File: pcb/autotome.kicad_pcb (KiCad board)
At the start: 2 copper layers, 61 parts, among them SW1 SW_PUSH, SW10 SW_PUSH, SW11 SW_PUSH, SW12 SW_PUSH, SW13 SW_PUSH, SW14 SW_PUSH, SW15 SW_PUSH, SW16 SW_PUSH, SW17 SW_PUSH, SW18 SW_PUSH, SW19 SW_PUSH, SW2 SW_PUSH, SW20 SW_PUSH, SW21 SW_PUSH, SW22 SW_PUSH, SW23 SW_PUSH, SW24 SW_PUSH, SW25 RotaryEncoder_Switch, SW27 SW_PUSH, SW28 SW_PUSH, SW29 SW_PUSH, SW3 SW_PUSH, SW30 SW_PUSH, SW31 SW_SPDT, SW4 SW_PUSH, SW5 SW_PUSH, SW6 SW_PUSH, SW7 SW_PUSH, SW8 SW_PUSH, SW9 SW_PUSH, U1 ProMicro

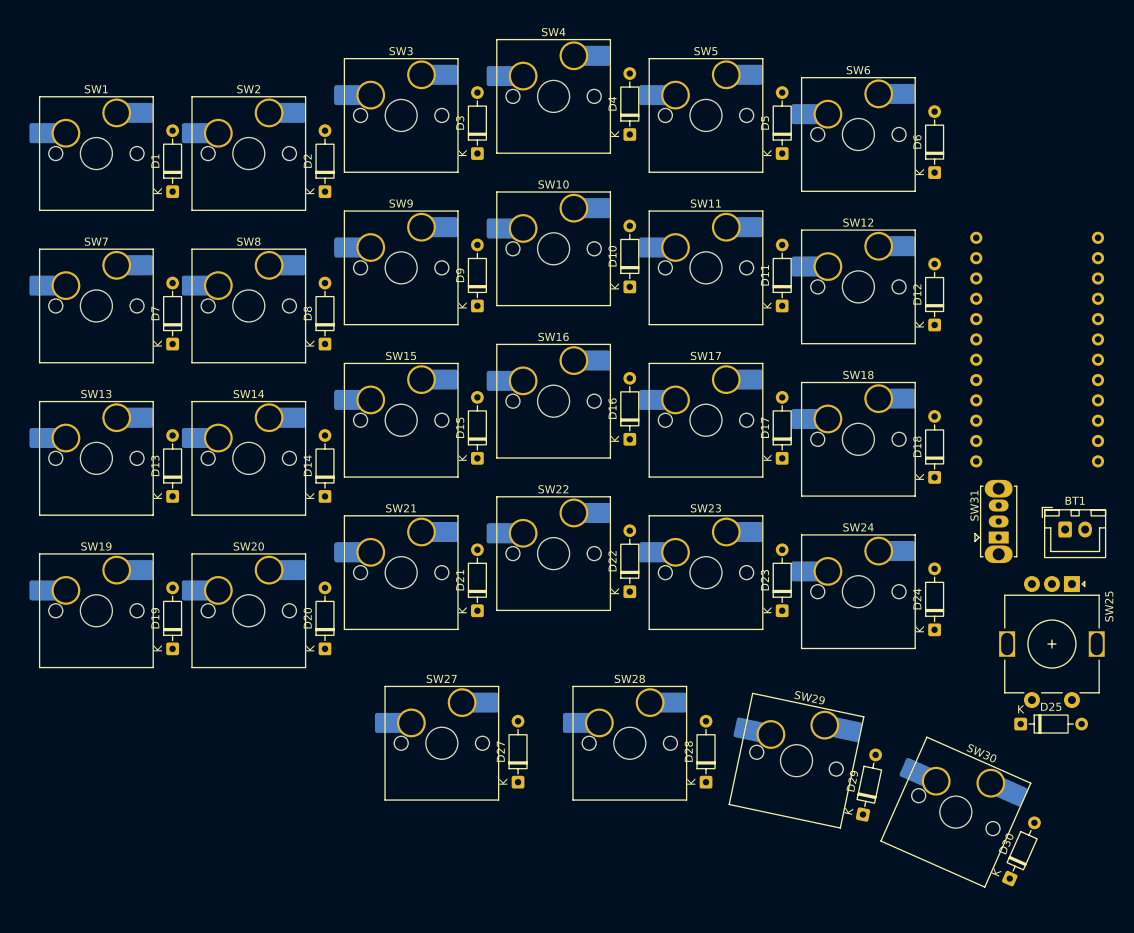
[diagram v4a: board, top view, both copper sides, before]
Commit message: add board outline at .5mm offset
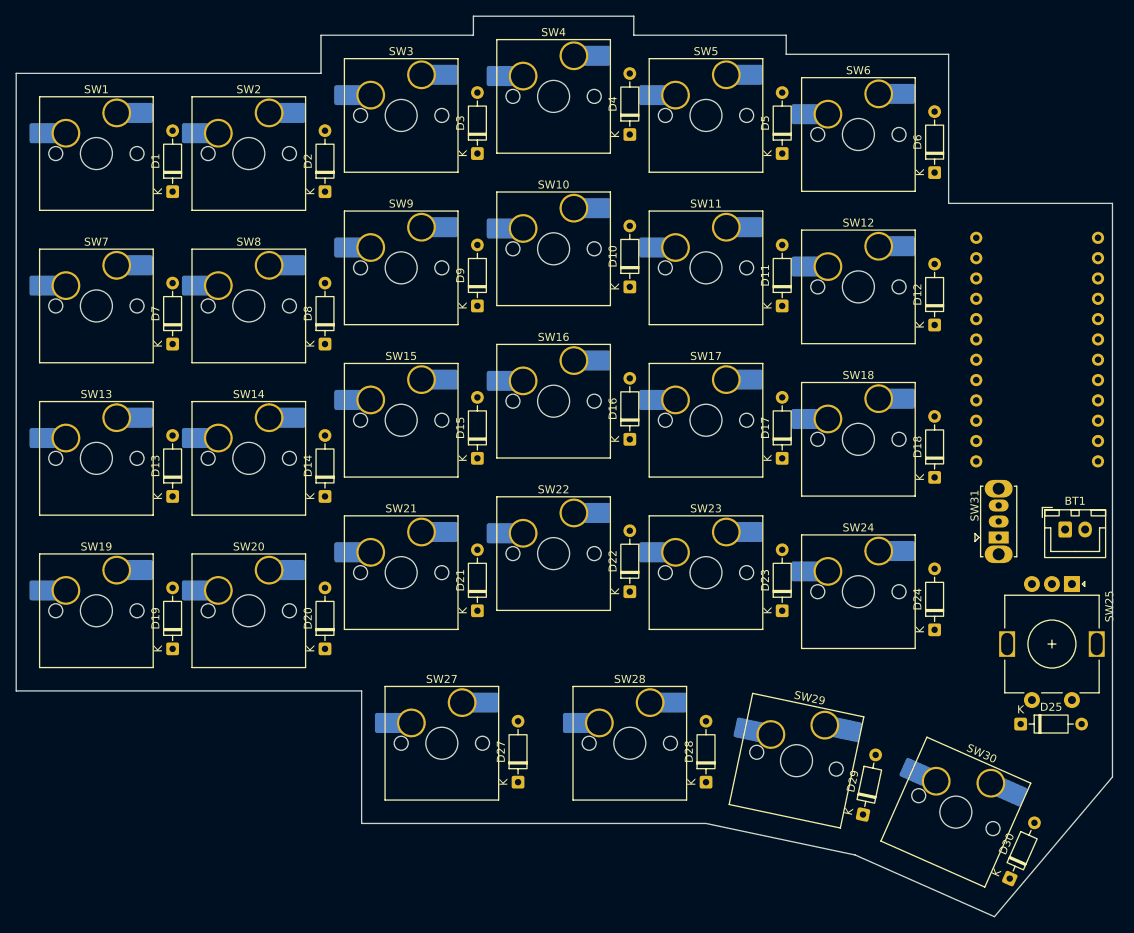
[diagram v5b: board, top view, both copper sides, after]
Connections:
- SW31 pad 1: Net-(BT1-+) -> unconnected-(SW31-A-Pad1)
- SW31 pad 2: unconnected-(SW31-B-Pad2) -> Net-(BT1-+)
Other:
- board outline added: 137 x 112.6 mm
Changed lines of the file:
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@@
 		(capping no)
 		(filling no)
-		(aux_axis_origin 123.14608 139.584744)
+		(grid_origin 136.967258 59.116053)
 		(pcbplotparams
 			(layerselection 0x00000000_00000000_55555555_5755f5ff)
@@
 		(duplicate_pad_numbers_are_jumpers no)
 		(fp_line
-			(start 2.289999 -1.12)
+			(start 2.289998 -1.12)
 			(end 2.290001 1.12)
 			(stroke
@@
 		(fp_line
 			(start 0 0)
-			(end 1.81 0.000001)
+			(end 1.81 0.000002)
 			(stroke
 				(width 0.1)
@@
 		)
 		(fp_line
-			(start -6.999999 7.000001)
+			(start -6.999999 7.000002)
 			(end -7 6)
 			(stroke
@@
 		(fp_line
 			(start -7 -6)
-			(end -7.000001 -6.999999)
+			(end -7.000002 -6.999999)
 			(stroke
 				(width 0.1)
@@
 		)
 		(fp_line
-			(start -7.000001 -6.999999)
-			(end 6.999999 -7.000001)
+			(start -7.000002 -6.999999)
+			(end 6.999999 -7.000002)
 			(stroke
 				(width 0.1)
@@
 		)
 		(fp_line
-			(start 7.000001 6.999999)
-			(end -6.999999 7.000001)
+			(start 7.000002 6.999999)
+			(end -6.999999 7.000002)
 			(stroke
 				(width 0.1)
@@
 		(fp_line
 			(start 7 6)
-			(end 7.000001 6.999999)
+			(end 7.000002 6.999999)
 			(stroke
 				(width 0.1)
@@
 		)
 		(fp_line
-			(start 6.999999 -7.000001)
+			(start 6.999999 -7.000002)
 			(end 7 -6)
 			(stroke
@@
 		)
 		(fp_line
-			(start -6.999999 7.000001)
-			(end 7.000001 6.999999)
+			(start -6.999999 7.000002)
+			(end 7.000002 6.999999)
 			(stroke
 				(width 0.1)
@@
 		)
 		(fp_line
-			(start -7.000001 -6.999999)
-			(end -6.999999 7.000001)
+			(start -7.000002 -6.999999)
+			(end -6.999999 7.000002)
 			(stroke
 				(width 0.1)
@@
 		)
 		(fp_line
-			(start 7.000001 6.999999)
-			(end 6.999999 -7.000001)
+			(start 7.000002 6.999999)
+			(end 6.999999 -7.000002)
 			(stroke
 				(width 0.1)
@@
 		)
 		(fp_line
-			(start 6.999999 -7.000001)
-			(end -7.000001 -6.999999)
+			(start 6.999999 -7.000002)
+			(end -7.000002 -6.999999)
 			(stroke
 				(width 0.1)
@@
 			(layers "*.Cu" "*.Mask")
 			(remove_unused_layers no)
-			(net "Net-(BT1-+)")
+			(net "unconnected-(SW31-A-Pad1)")
 			(pinfunction "A_1")
 			(pintype "passive")
@@
 			(layers "*.Cu" "*.Mask")
 			(remove_unused_layers no)
-			(net "unconnected-(SW31-B-Pad2)")
+			(net "Net-(BT1-+)")
 			(pinfunction "B_2")
 			(pintype "passive")
@@
 		(sheetname "/")
 		(sheetfile "autotome.kicad_sch")
+		(units
+			(unit
+				(name "A")
+				(pins "1" "2" "3" "4" "5" "6" "7" "8" "9" "10" "11" "12" "24" "23" "22"
+					"21" "20" "19" "18" "17" "16" "15" "14" "13"
+				)
+			)
+		)
 		(attr through_hole)
 		(duplicate_pad_numbers_are_jumpers no)
@@
 		)
 	)
+	(gr_line
+		(start 18.232504 42.362516)
+		(end 56.332504 42.362516)
+		(stroke
+			(width 0.05)
+			(type default)
+		)
+		(layer "Edge.Cuts")
+	)
+	(gr_line
+		(start 18.232504 119.562516)
+		(end 18.232504 42.362516)
+		(stroke
+			(width 0.05)
+			(type default)
+		)
+		(layer "Edge.Cuts")
+	)
+	(gr_line
+		(start 18.232504 119.562516)
+		(end 61.412503 119.562516)
+		(stroke
+			(width 0.05)
+			(type default)
+		)
+		(layer "Edge.Cuts")
+	)
+	(gr_line
+		(start 56.332504 37.599507)
+		(end 75.382498 37.599507)
+		(stroke
+			(width 0.05)
+			(type default)
+		)
+		(layer "Edge.Cuts")
+	)
+	(gr_line
+		(start 56.332504 42.362516)
+		(end 56.332504 37.599507)
+		(stroke
+			(width 0.05)
+			(type default)
+		)
+		(layer "Edge.Cuts")
+	)
+	(gr_line
+		(start 61.412503 119.562516)
+		(end 61.412503 136.125497)
+		(stroke
+			(width 0.05)
+			(type default)
+		)
+		(layer "Edge.Cuts")
+	)
+	(gr_line
+		(start 61.412503 136.125497)
+		(end 104.460011 136.125491)
+		(stroke
+			(width 0.05)
+			(type default)
+		)
+		(layer "Edge.Cuts")
+	)
+	(gr_line
+		(start 75.382503 35.218496)
+		(end 75.382498 37.599507)
+		(stroke
+			(width 0.05)
+			(type default)
+		)
+		(layer "Edge.Cuts")
+	)
+	(gr_line
+		(start 75.382503 35.218496)
+		(end 95.432503 35.218496)
+		(stroke
+			(width 0.05)
+			(type default)
+		)
+		(layer "Edge.Cuts")
+	)
+	(gr_line
+		(start 95.432498 37.599507)
+		(end 114.482498 37.599507)
+		(stroke
+			(width 0.05)
+			(type default)
+		)
+		(layer "Edge.Cuts")
+	)
+	(gr_line
+		(start 95.432503 35.218496)
+		(end 95.432498 37.599507)
+		(stroke
+			(width 0.05)
+			(type default)
+		)
+		(layer "Edge.Cuts")
+	)
+	(gr_line
+		(start 104.460011 136.125491)
+		(end 123.09786 140.066693)
+		(stroke
+			(width 0.05)
+			(type default)
+		)
+		(layer "Edge.Cuts")
+	)
+	(gr_line
+		(start 114.482498 37.599507)
+		(end 114.482515 39.980505)
+		(stroke
+			(width 0.05)
+			(type default)
+		)
+		(layer "Edge.Cuts")
+	)
+	(gr_line
+		(start 114.482515 39.980505)
+		(end 134.785011 39.980505)
+		(stroke
+			(width 0.05)
+			(type default)
+		)
+		(layer "Edge.Cuts")
+	)
+	(gr_line
+		(start 123.09786 140.066693)
+		(end 140.517091 147.77856)
+		(stroke
+			(width 0.05)
+			(type default)
+		)
+		(layer "Edge.Cuts")
+	)
+	(gr_line
+		(start 134.785011 39.980505)
+		(end 134.785011 58.616053)
+		(stroke
+			(width 0.05)
+			(type default)
+		)
+		(layer "Edge.Cuts")
+	)
+	(gr_line
+		(start 134.785011 58.616053)
+		(end 155.267258 58.616053)
+		(stroke
+			(width 0.05)
+			(type default)
+		)
+		(layer "Edge.Cuts")
+	)
+	(gr_line
+		(start 155.267258 58.616053)
+		(end 155.267258 130.316053)
+		(stroke
+			(width 0.05)
+			(type default)
+		)
+		(layer "Edge.Cuts")
+	)
+	(gr_line
+		(start 155.267258 130.316053)
+		(end 140.517091 147.77856)
+		(stroke
+			(width 0.05)
+			(type default)
+		)
+		(layer "Edge.Cuts")
+	)
 	(embedded_fonts no)

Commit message: add 1mm fillet
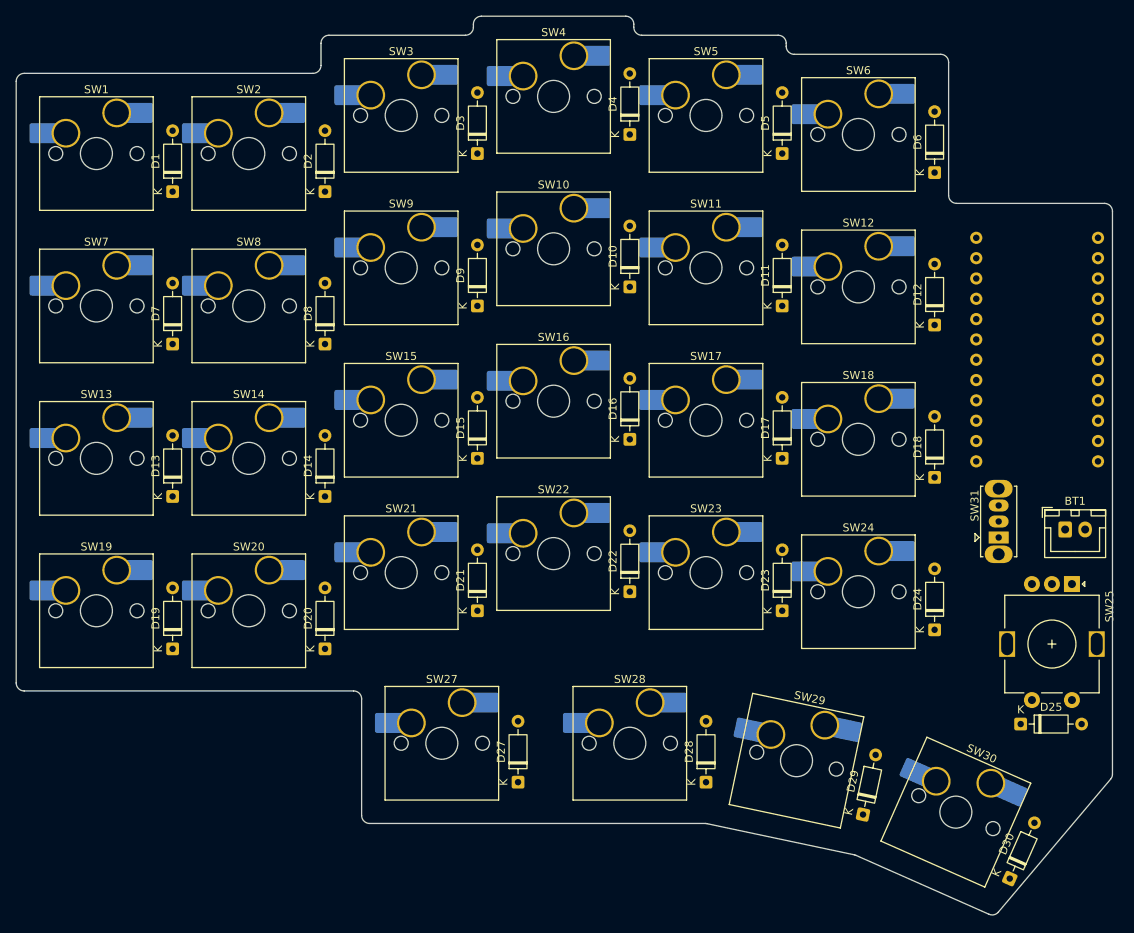
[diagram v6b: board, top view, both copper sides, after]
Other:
- board size 137 x 112.6 mm -> 137 x 112.3 mm

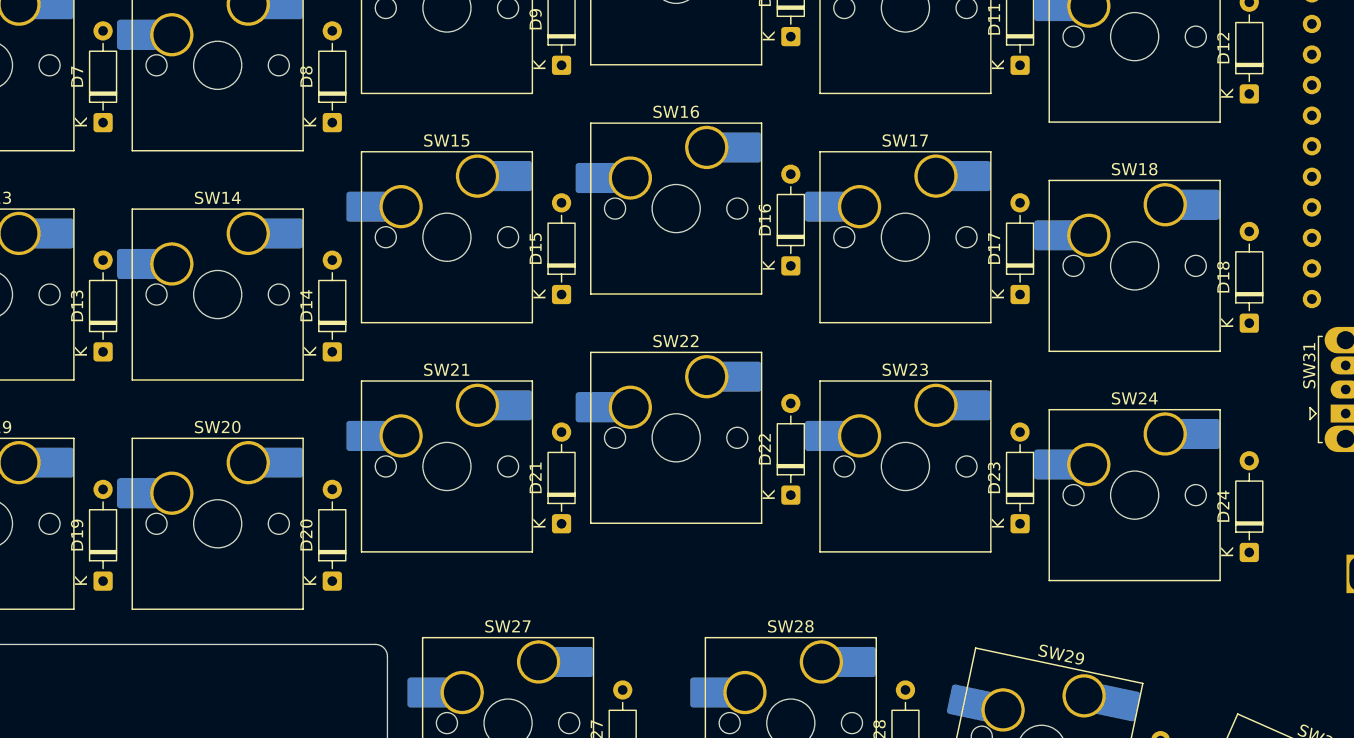
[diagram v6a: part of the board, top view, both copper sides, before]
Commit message: add 4 m3 screw holes
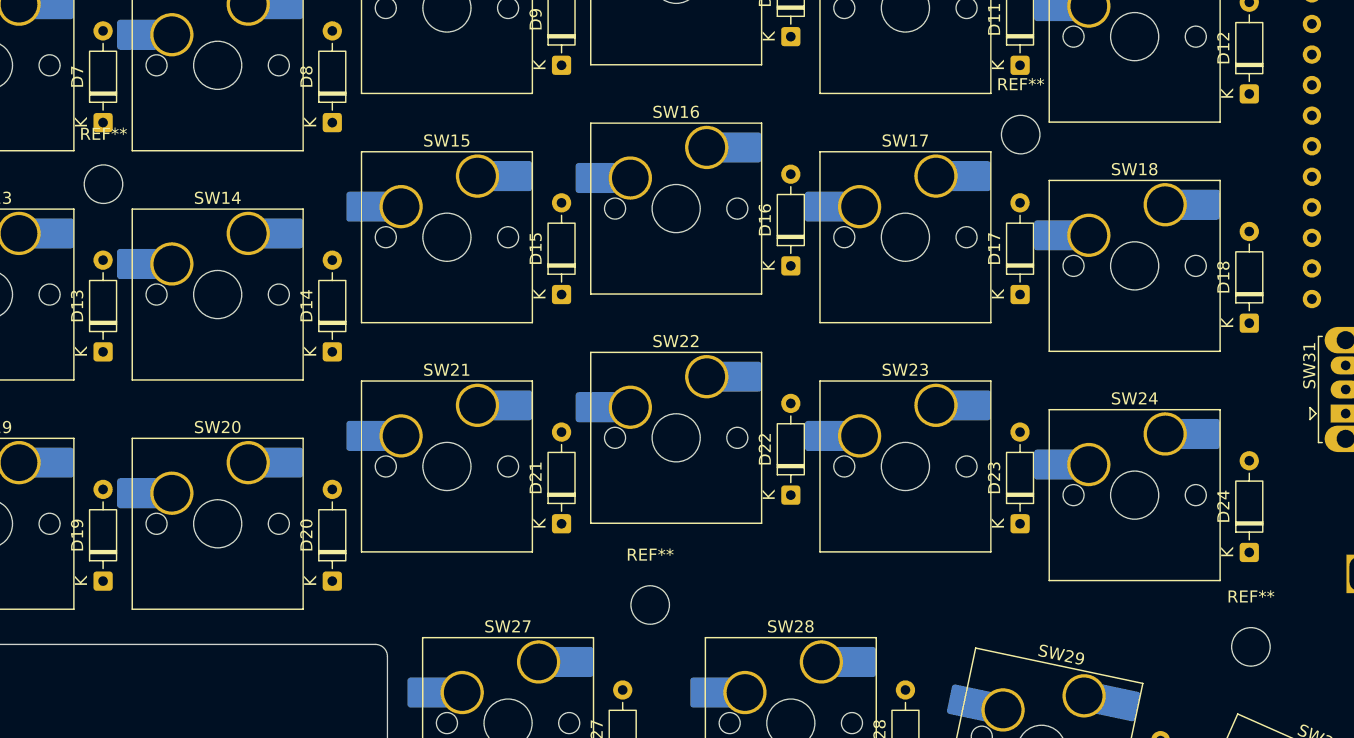
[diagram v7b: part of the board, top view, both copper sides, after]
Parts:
- added REF**: MountingHole_3.2mm_M3, MountingHole:MountingHole_3.2mm_M3, F.Cu at (83.2, 116.3)
- added REF**: MountingHole_3.2mm_M3, MountingHole:MountingHole_3.2mm_M3, F.Cu at (114.0, 77.2)
- added REF**: MountingHole_3.2mm_M3, MountingHole:MountingHole_3.2mm_M3, F.Cu at (37.8, 81.3)
- added REF**: MountingHole_3.2mm_M3, MountingHole:MountingHole_3.2mm_M3, F.Cu at (133.2, 119.8)

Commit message: add cutout for breakaway
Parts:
- moved D1 4.00 mm to (37.8, 53.1)
- moved D2 4.00 mm to (56.8, 53.1)
- moved D6 3.00 mm to (133.0, 51.8)
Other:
- outline, holes or cut-outs redrawn
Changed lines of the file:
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@@
 		(capping no)
 		(filling no)
-		(grid_origin 136.967258 59.116053)
 		(pcbplotparams
 			(layerselection 0x00000000_00000000_55555555_5755f5ff)
@@
 	(footprint "Diode_THT:D_DO-35_SOD27_P7.62mm_Horizontal"
 		(layer "F.Cu")
-		(at 37.7825 57.15 90)
+		(at 37.7825 53.15 90)
 		(descr "Diode, DO-35_SOD27 series, Axial, Horizontal, pin pitch=7.62mm, length*diameter=4*2mm^2, http://www.diodes.com/_files/packages/DO-35.pdf")
 		(tags "Diode DO-35_SOD27 series Axial Horizontal pin pitch 7.62mm  length 4mm diameter 2mm")
@@
 	(footprint "Diode_THT:D_DO-35_SOD27_P7.62mm_Horizontal"
 		(layer "F.Cu")
-		(at 56.8325 57.15 90)
+		(at 56.8325 53.15 90)
 		(descr "Diode, DO-35_SOD27 series, Axial, Horizontal, pin pitch=7.62mm, length*diameter=4*2mm^2, http://www.diodes.com/_files/packages/DO-35.pdf")
 		(tags "Diode DO-35_SOD27 series Axial Horizontal pin pitch 7.62mm  length 4mm diameter 2mm")
@@
 	(footprint "Diode_THT:D_DO-35_SOD27_P7.62mm_Horizontal"
 		(layer "F.Cu")
-		(at 133.0325 54.768 90)
+		(at 133.0325 51.768 90)
 		(descr "Diode, DO-35_SOD27 series, Axial, Horizontal, pin pitch=7.62mm, length*diameter=4*2mm^2, http://www.diodes.com/_files/packages/DO-35.pdf")
 		(tags "Diode DO-35_SOD27 series Axial Horizontal pin pitch 7.62mm  length 4mm diameter 2mm")
@@
 	)
 	(gr_line
-		(start 18.232504 118.562516)
+		(start 18.232504 54.62)
 		(end 18.232504 43.362516)
 		(stroke
@@
 	)
 	(gr_line
+		(start 18.232504 118.562516)
+		(end 18.232504 56.616053)
+		(stroke
+			(width 0.05)
+			(type default)
+		)
+		(layer "Edge.Cuts")
+	)
+	(gr_line
 		(start 19.232504 42.362516)
 		(end 55.332504 42.362516)
@@
 	(gr_line
 		(start 134.785011 40.980505)
+		(end 134.8 54.62)
+		(stroke
+			(width 0.05)
+			(type default)
+		)
+		(layer "Edge.Cuts")
+	)
+	(gr_line
+		(start 134.785011 56.616053)
+		(end 18.232504 56.616053)
+		(stroke
+			(width 0.05)
+			(type default)
+		)
+		(layer "Edge.Cuts")
+	)
+	(gr_line
+		(start 134.785011 56.616053)
 		(end 134.785011 57.616053)
 		(stroke
 			(width 0.05)
+			(type default)
+		)
+		(layer "Edge.Cuts")
+	)
+	(gr_line
+		(start 134.8 54.62)
+		(end 18.232504 54.62)
+		(stroke
+			(width 0.05)
